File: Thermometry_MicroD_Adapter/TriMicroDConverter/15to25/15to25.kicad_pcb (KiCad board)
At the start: 2 copper layers, 69.1 x 8.7 mm, 3 parts, among them J1 Conn_02x05_Odd_Even, J2 DB15_Male, J4 DB25_Male

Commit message: Updated Gerber
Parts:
- added ?: , , F.Cu at (18.0, 10.0)
- renumbered J4 to J1
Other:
- board text added: "TriMicroDConvert_15Pin_V1 August 2021 Ryan Morgenstern"
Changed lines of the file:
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@@
   (general
     (thickness 1.6)
-    (drawings 4)
+    (drawings 6)
     (tracks 96)
     (zones 0)
-    (modules 3)
+    (modules 4)
     (nets 27)
   )
@@
     (add_net "Net-(J4-Pad13)")
   )
+  (module "" (layer F.Cu)
+    (at 18 10)
+    (fp_text reference "" (at -32 0.55) (layer F.SilkS)
+      (effects (font (size 1.27 1.27) (thickness 0.15)))
+    )
+    (fp_text value "" (at -32 0.55) (layer F.SilkS)
+      (effects (font (size 1.27 1.27) (thickness 0.15)))
+    )
+    (fp_text user J1 (at -50 -7 -180) (layer F.SilkS)
+      (effects (font (size 1.2 1.2) (thickness 0.15)))
+    )
+  )
   (module Connector:Norcomp-380-025-113L001-microd_NoLeads (layer B.Cu)
     (at -32 0.55 180)
     (tags "380-025-213L001 ")
-    (fp_text reference J4 (at 0 -2.71) (layer B.SilkS)
-      (effects (font (size 1.2 1.2) (thickness 0.15)))
+    (fp_text reference J1 (at 0 -2.71) (layer B.SilkS)
+      (effects (font (size 1.2 1.2) (thickness 0.15)) (justify mirror))
     )
     (fp_text value DB25_Male (at 0.365 -6) (layer F.Fab)
       (effects (font (size 1.2 1.2) (thickness 0.15)))
     )
+    (fp_line (start -14.85 3.675) (end -14.85 -3.675) (layer B.CrtYd) (width 0.15))
+    (fp_line (start 14.85 3.675) (end -14.85 3.675) (layer B.CrtYd) (width 0.15))
+    (fp_line (start 14.85 -3.675) (end 14.85 3.675) (layer B.CrtYd) (width 0.15))
+    (fp_line (start -14.85 -3.675) (end 14.85 -3.675) (layer B.CrtYd) (width 0.15))
+    (fp_line (start 9.08 1.51) (end -8.08 1.51) (layer B.SilkS) (width 0.15))
+    (fp_line (start 9.08 -1.51) (end 9.08 1.51) (layer B.SilkS) (width 0.15))
+    (fp_line (start -9.08 -1.51) (end 9.08 -1.51) (layer B.SilkS) (width 0.15))
+    (fp_line (start -9.08 0.51) (end -9.08 -1.51) (layer B.SilkS) (width 0.15))
     (fp_line (start -8.08 1.51) (end -9.08 0.51) (layer B.SilkS) (width 0.15))
-    (fp_line (start -9.08 0.51) (end -9.08 -1.51) (layer B.SilkS) (width 0.15))
-    (fp_line (start -9.08 -1.51) (end 9.08 -1.51) (layer B.SilkS) (width 0.15))
-    (fp_line (start 9.08 -1.51) (end 9.08 1.51) (layer B.SilkS) (width 0.15))
-    (fp_line (start 9.08 1.51) (end -8.08 1.51) (layer B.SilkS) (width 0.15))
-    (fp_line (start -14.85 -3.675) (end 14.85 -3.675) (layer B.CrtYd) (width 0.15))
-    (fp_line (start 14.85 -3.675) (end 14.85 3.675) (layer B.CrtYd) (width 0.15))
-    (fp_line (start 14.85 3.675) (end -14.85 3.675) (layer B.CrtYd) (width 0.15))
-    (fp_line (start -14.85 3.675) (end -14.85 -3.675) (layer B.CrtYd) (width 0.15))
     (fp_text user "Male / Plug" (at 0 2.54) (layer B.Fab)
       (effects (font (size 1.2 1.2) (thickness 0.15)) (justify mirror))
@@
       (rotate (xyz 0 0 180))
     )
+    (model C:/Users/Cir/Downloads/380-025-113L001.STEP
+      (offset (xyz 0 3.6 10.5))
+      (scale (xyz 1 1 1))
+      (rotate (xyz 0 0 0))
+    )
   )
   (module Connector_PinHeader_1.00mm:PinHeader_2x05_P1.00mm_Vertical (layer F.Cu)
@@
     (descr "Through hole straight pin header, 2x05, 1.00mm pitch, double rows")
     (tags "Through hole pin header THT 2x05 1.00mm double row")
-    (fp_text reference J1 (at -1.9 5.8) (layer F.SilkS)
+    (fp_text reference J1 (at 3.07 -0.29) (layer F.SilkS)
       (effects (font (size 1 1) (thickness 0.15)))
     )
@@
       (effects (font (size 1 1) (thickness 0.15)))
     )
+    (fp_line (start -0.075 -0.5) (end 1.65 -0.5) (layer F.Fab) (width 0.1))
+    (fp_line (start 1.65 -0.5) (end 1.65 4.5) (layer F.Fab) (width 0.1))
+    (fp_line (start 1.65 4.5) (end -0.65 4.5) (layer F.Fab) (width 0.1))
+    (fp_line (start -0.65 4.5) (end -0.65 0.075) (layer F.Fab) (width 0.1))
+    (fp_line (start -0.65 0.075) (end -0.075 -0.5) (layer F.Fab) (width 0.1))
+    (fp_line (start -0.71 4.56) (end -0.394493 4.56) (layer F.SilkS) (width 0.12))
+    (fp_line (start 1.394493 4.56) (end 1.71 4.56) (layer F.SilkS) (width 0.12))
+    (fp_line (start 0.394493 4.56) (end 0.605507 4.56) (layer F.SilkS) (width 0.12))
+    (fp_line (start -0.71 0.685) (end -0.71 4.56) (layer F.SilkS) (width 0.12))
+    (fp_line (start 1.71 -0.56) (end 1.71 4.56) (layer F.SilkS) (width 0.12))
+    (fp_line (start -0.71 0.685) (end -0.608276 0.685) (layer F.SilkS) (width 0.12))
+    (fp_line (start 1.394493 -0.56) (end 1.71 -0.56) (layer F.SilkS) (width 0.12))
+    (fp_line (start -0.71 0) (end -0.71 -0.685) (layer F.SilkS) (width 0.12))
+    (fp_line (start -0.71 -0.685) (end 0 -0.685) (layer F.SilkS) (width 0.12))
+    (fp_line (start -1.15 -1) (end -1.15 5) (layer F.CrtYd) (width 0.05))
+    (fp_line (start -1.15 5) (end 2.15 5) (layer F.CrtYd) (width 0.05))
+    (fp_line (start 2.15 5) (end 2.15 -1) (layer F.CrtYd) (width 0.05))
     (fp_line (start 2.15 -1) (end -1.15 -1) (layer F.CrtYd) (width 0.05))
-    (fp_line (start 2.15 5) (end 2.15 -1) (layer F.CrtYd) (width 0.05))
-    (fp_line (start -1.15 5) (end 2.15 5) (layer F.CrtYd) (width 0.05))
-    (fp_line (start -1.15 -1) (end -1.15 5) (layer F.CrtYd) (width 0.05))
-    (fp_line (start -0.71 -0.685) (end 0 -0.685) (layer F.SilkS) (width 0.12))
-    (fp_line (start -0.71 0) (end -0.71 -0.685) (layer F.SilkS) (width 0.12))
-    (fp_line (start 1.394493 -0.56) (end 1.71 -0.56) (layer F.SilkS) (width 0.12))
-    (fp_line (start -0.71 0.685) (end -0.608276 0.685) (layer F.SilkS) (width 0.12))
-    (fp_line (start 1.71 -0.56) (end 1.71 4.56) (layer F.SilkS) (width 0.12))
-    (fp_line (start -0.71 0.685) (end -0.71 4.56) (layer F.SilkS) (width 0.12))
-    (fp_line (start 0.394493 4.56) (end 0.605507 4.56) (layer F.SilkS) (width 0.12))
-    (fp_line (start 1.394493 4.56) (end 1.71 4.56) (layer F.SilkS) (width 0.12))
-    (fp_line (start -0.71 4.56) (end -0.394493 4.56) (layer F.SilkS) (width 0.12))
-    (fp_line (start -0.65 0.075) (end -0.075 -0.5) (layer F.Fab) (width 0.1))
-    (fp_line (start -0.65 4.5) (end -0.65 0.075) (layer F.Fab) (width 0.1))
-    (fp_line (start 1.65 4.5) (end -0.65 4.5) (layer F.Fab) (width 0.1))
-    (fp_line (start 1.65 -0.5) (end 1.65 4.5) (layer F.Fab) (width 0.1))
-    (fp_line (start -0.075 -0.5) (end 1.65 -0.5) (layer F.Fab) (width 0.1))
     (fp_text user %R (at 0.5 2) (layer F.Fab)
       (effects (font (size 1 1) (thickness 0.15)))
@@
       (effects (font (size 1 1) (thickness 0.15)) (justify mirror))
     )
-    (fp_line (start 16.4465 -4.5466) (end 16.4465 3.4544) (layer B.CrtYd) (width 0.05))
-    (fp_line (start -7.5565 -4.5466) (end 16.4465 -4.5466) (layer B.CrtYd) (width 0.05))
-    (fp_line (start -7.5565 3.4544) (end -7.5565 -4.5466) (layer B.CrtYd) (width 0.05))
-    (fp_line (start 16.4465 3.4544) (end -7.5565 3.4544) (layer B.CrtYd) (width 0.05))
+    (fp_line (start -7.4295 -4.4196) (end 16.3195 -4.4196) (layer B.SilkS) (width 0.12))
+    (fp_line (start 16.3195 -4.4196) (end 16.3195 3.3274) (layer B.SilkS) (width 0.12))
+    (fp_line (start 16.3195 3.3274) (end -7.4295 3.3274) (layer B.SilkS) (width 0.12))
+    (fp_line (start -7.4295 3.3274) (end -7.4295 -4.4196) (layer B.SilkS) (width 0.12))
+    (fp_line (start -7.3025 -4.2926) (end 16.1925 -4.2926) (layer B.Fab) (width 0.1))
+    (fp_line (start 16.1925 -4.2926) (end 16.1925 3.2004) (layer B.Fab) (width 0.1))
+    (fp_line (start 16.1925 3.2004) (end -7.3025 3.2004) (layer B.Fab) (width 0.1))
+    (fp_line (start -7.3025 3.2004) (end -7.3025 -4.2926) (layer B.Fab) (width 0.1))
+    (fp_line (start 4.318 3.0734) (end 4.572 3.0734) (layer B.SilkS) (width 0.12))
+    (fp_line (start 4.572 3.0734) (end 4.572 3.3274) (layer B.SilkS) (width 0.12))
+    (fp_line (start 4.572 3.3274) (end 4.318 3.3274) (layer B.SilkS) (width 0.12))
+    (fp_line (start 4.318 3.3274) (end 4.318 3.0734) (layer B.SilkS) (width 0.12))
     (fp_line (start 4.445 3.2004) (end 4.445 3.2004) (layer B.Fab) (width 0.1))
     (fp_line (start 4.445 3.2004) (end 4.445 3.2004) (layer B.Fab) (width 0.1))
     (fp_line (start 4.445 3.2004) (end 4.445 3.2004) (layer B.Fab) (width 0.1))
     (fp_line (start 4.445 3.2004) (end 4.445 3.2004) (layer B.Fab) (width 0.1))
-    (fp_line (start 4.318 3.3274) (end 4.318 3.0734) (layer B.SilkS) (width 0.12))
-    (fp_line (start 4.572 3.3274) (end 4.318 3.3274) (layer B.SilkS) (width 0.12))
-    (fp_line (start 4.572 3.0734) (end 4.572 3.3274) (layer B.SilkS) (width 0.12))
-    (fp_line (start 4.318 3.0734) (end 4.572 3.0734) (layer B.SilkS) (width 0.12))
-    (fp_line (start -7.3025 3.2004) (end -7.3025 -4.2926) (layer B.Fab) (width 0.1))
-    (fp_line (start 16.1925 3.2004) (end -7.3025 3.2004) (layer B.Fab) (width 0.1))
-    (fp_line (start 16.1925 -4.2926) (end 16.1925 3.2004) (layer B.Fab) (width 0.1))
-    (fp_line (start -7.3025 -4.2926) (end 16.1925 -4.2926) (layer B.Fab) (width 0.1))
-    (fp_line (start -7.4295 3.3274) (end -7.4295 -4.4196) (layer B.SilkS) (width 0.12))
-    (fp_line (start 16.3195 3.3274) (end -7.4295 3.3274) (layer B.SilkS) (width 0.12))
-    (fp_line (start 16.3195 -4.4196) (end 16.3195 3.3274) (layer B.SilkS) (width 0.12))
-    (fp_line (start -7.4295 -4.4196) (end 16.3195 -4.4196) (layer B.SilkS) (width 0.12))
+    (fp_line (start 16.4465 3.4544) (end -7.5565 3.4544) (layer B.CrtYd) (width 0.05))
+    (fp_line (start -7.5565 3.4544) (end -7.5565 -4.5466) (layer B.CrtYd) (width 0.05))
+    (fp_line (start -7.5565 -4.5466) (end 16.4465 -4.5466) (layer B.CrtYd) (width 0.05))
+    (fp_line (start 16.4465 -4.5466) (end 16.4465 3.4544) (layer B.CrtYd) (width 0.05))
     (fp_text user * (at -2.54 0) (layer B.Fab)
       (effects (font (size 1 1) (thickness 0.15)) (justify mirror))
@@
     )
   )
+  (gr_text "TriMicroDConvert_15Pin_V1\nAugust 2021\nRyan Morgenstern" (at -51.66 3.41) (layer B.SilkS)
+    (effects (font (size 0.4 0.4) (thickness 0.1)) (justify mirror))
+  )
+  (gr_text "TriMicroDConvert_15Pin_V1\nAugust 2021\nRyan Morgenstern" (at -51.4 3.36) (layer F.SilkS)
+    (effects (font (size 0.4 0.4) (thickness 0.1)))
+  )
   (gr_line (start -56.1 -3.8) (end 13 -3.8) (layer Edge.Cuts) (width 0.15))

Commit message: update
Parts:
- renumbered J1 to J4
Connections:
- J4 pad 3: Net-(J2-Pad3) -> Net-(J2-Pad4)
- J4 pad 4: Net-(J2-Pad4) -> Net-(J2-Pad5)
- J4 pad 5: Net-(J2-Pad5) -> Net-(J2-Pad6)
- J4 pad 6: Net-(J2-Pad6) -> Net-(J2-Pad7)
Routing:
- net Net-(J2-Pad7): track 0.00 -> 37.3 mm
- net Net-(J2-Pad3): track 27.5 -> 0.00 mm
- net Net-(J2-Pad4): track 30.6 -> 29.2 mm
- net Net-(J2-Pad1): track 21.3 -> 22.4 mm
- net Net-(J2-Pad6): track 35.5 -> 34.6 mm
- net Net-(J2-Pad5): track 32.8 -> 31.9 mm
- net Net-(J1-Pad2): track 23.3 -> 23.9 mm
- net Net-(J1-Pad1): track 23.9 -> 24.5 mm
- net Net-(J1-Pad10): track 13.6 -> 13.0 mm
- net Net-(J2-Pad11): track 28.7 -> 29.3 mm
- net Net-(J2-Pad9): track 23.4 -> 23.9 mm
- net Net-(J2-Pad2): track 24.8 -> 25.3 mm
- net Net-(J2-Pad8): track 39.5 -> 40.0 mm
- net Net-(J2-Pad10): track 26.0 -> 26.5 mm
- net Net-(J2-Pad12): track 31.4 -> 31.9 mm
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
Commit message: update
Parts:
- removed ?: , 
- added J3: Conn_01x04, Connector_JST:JST_PH_B4B-PH-K_1x04_P2.00mm_Vertical, F.Cu at (-62.5, 0.00)
- added J5: Conn_01x02, Connector_PinHeader_1.00mm:PinHeader_1x02_P1.00mm_Vertical, F.Cu at (-51.1, 0.01)
- J1: value Conn_02x05_Odd_Even -> Conn_01x04; footprint Connector_PinHeader_1.00mm:PinHeader_2x05_P1.00mm_Vertical -> Connector_JST:JST_PH_B4B-PH-K_1x04_P2.00mm_Vertical
- moved J1 21.0 mm to (-75.5, 0.00), turned to 0 degrees
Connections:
- J4 pad 10: Net-(J1-Pad5) -> Net-(J3-Pad1)
- J4 pad 11: Net-(J1-Pad7) -> Net-(J3-Pad3)
- J4 pad 12: Net-(J1-Pad9) -> Net-(J4-Pad12)
- J4 pad 23: Net-(J1-Pad6) -> Net-(J3-Pad2)
- J4 pad 24: Net-(J1-Pad8) -> Net-(J3-Pad4)
- J4 pad 25: Net-(J1-Pad10) -> Net-(J4-Pad25)
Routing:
- net Net-(J3-Pad1): track 0.00 -> 28.4 mm
- net Net-(J3-Pad2): track 0.00 -> 26.2 mm
- net Net-(J3-Pad3): track 0.00 -> 23.0 mm
- net Net-(J3-Pad4): track 0.00 -> 20.8 mm
- net Net-(J1-Pad1): track 24.5 -> 44.2 mm
- net Net-(J1-Pad5): track 19.1 -> 0.00 mm
- net Net-(J1-Pad6): track 18.4 -> 0.00 mm
- net Net-(J1-Pad2): track 23.9 -> 42.1 mm
- net Net-(J1-Pad3): track 21.8 -> 38.8 mm
- net Net-(J1-Pad7): track 16.4 -> 0.00 mm
- net Net-(J1-Pad8): track 15.7 -> 0.00 mm
- net Net-(J1-Pad4): track 21.2 -> 36.6 mm
- net Net-(J1-Pad9): track 14.3 -> 0.00 mm
- net Net-(J4-Pad12): track 0.00 -> 14.2 mm
- net Net-(J4-Pad25): track 0.00 -> 13.7 mm
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- added copper zone on F.Cu, net GND
- added copper zone on B.Cu, net Net-(J2-Pad12)
- removed copper zone on B.Cu, net (none)
- removed copper zone on F.Cu, net (none)
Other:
- board size 69.1 x 8.7 mm -> 91.9 x 8.7 mm
- board text added: "TriMicroDConvert_15Pin_V2 July 2022 Ryan Morgenstern"
- board text removed: "TriMicroDConvert_15Pin_V1 August 2021 Ryan Morgenstern"

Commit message: Update
Added current versions of adapter boards.
Added heater line splitter
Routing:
- added copper zone on In1.Cu, net GND
- added copper zone on In2.Cu, net GND
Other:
- copper layers 2 -> 4
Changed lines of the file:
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@@
   (layers
     (0 F.Cu signal)
+    (1 In1.Cu signal)
+    (2 In2.Cu signal)
     (31 B.Cu signal)
     (32 B.Adhes user)
@@
     (47 F.CrtYd user)
     (48 B.Fab user)
-    (49 F.Fab user hide)
+    (49 F.Fab user)
   )
   (setup
@@
       )
     )
+  )
+  (zone (net 21) (net_name GND) (layer In1.Cu) (hatch edge 0.508)
+    (connect_pads (clearance 0.4))
+    (min_thickness 0.254)
+    (fill yes (arc_segments 32) (thermal_gap 0.508) (thermal_bridge_width 0.508))
+    (polygon
+      (pts
+        (xy 16.8 9) (xy -80.5 9) (xy -80.5 -6.7) (xy 16.7 -6.7)
+      )
+    )
+  )
+  (zone (net 21) (net_name GND) (layer In2.Cu) (hatch edge 0.508)
+    (connect_pads (clearance 0.4))
+    (min_thickness 0.254)
+    (fill yes (arc_segments 32) (thermal_gap 0.508) (thermal_bridge_width 0.508))
+    (polygon
+      (pts
+        (xy 15.9 8) (xy -80.5 8) (xy -80.5 -6.9) (xy 15.9 -6.9)
+      )
+    )

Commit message: update
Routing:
- net Net-(J2-Pad6): track 34.8 -> 34.1 mm
- net Net-(J2-Pad5): track 32.0 -> 31.4 mm
- net Net-(J2-Pad8): track 40.2 -> 39.6 mm
- net Net-(J2-Pad7): track 37.4 -> 36.9 mm
- removed copper zone on In1.Cu, net GND
- removed copper zone on In2.Cu, net GND
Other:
- copper layers 4 -> 2
- net class Default: trace_width 0.09 -> 0.135

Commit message: update
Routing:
- added copper zone on B.Cu, net GND
- removed copper zone on B.Cu, net Net-(J2-Pad12)
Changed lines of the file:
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@@
     (mod_text_size 1 1)
     (mod_text_width 0.15)
-    (pad_size 1.1 1.1)
-    (pad_drill 0.61)
+    (pad_size 3.6 3.6)
+    (pad_drill 2.2606)
     (pad_to_mask_clearance 0)
     (aux_axis_origin 0 0)
@@
   (segment (start -49.34 -1.8) (end -51.15 0.01) (width 0.135) (layer F.Cu) (net 27))
   (segment (start -40.15 -1.8) (end -49.34 -1.8) (width 0.135) (layer F.Cu) (net 27))
-  (zone (net 8) (net_name "Net-(J2-Pad12)") (layer B.Cu) (hatch edge 0.508)
+  (zone (net 21) (net_name GND) (layer B.Cu) (hatch edge 0.508)
     (connect_pads (clearance 0.2))
     (min_thickness 0.254)

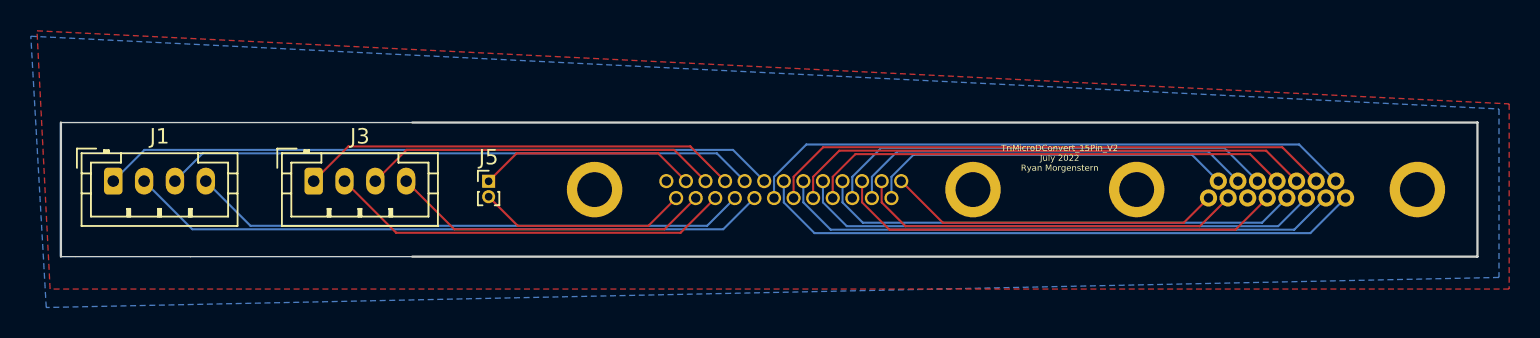
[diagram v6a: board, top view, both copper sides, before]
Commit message: Fixed Error in board. Added diagrams
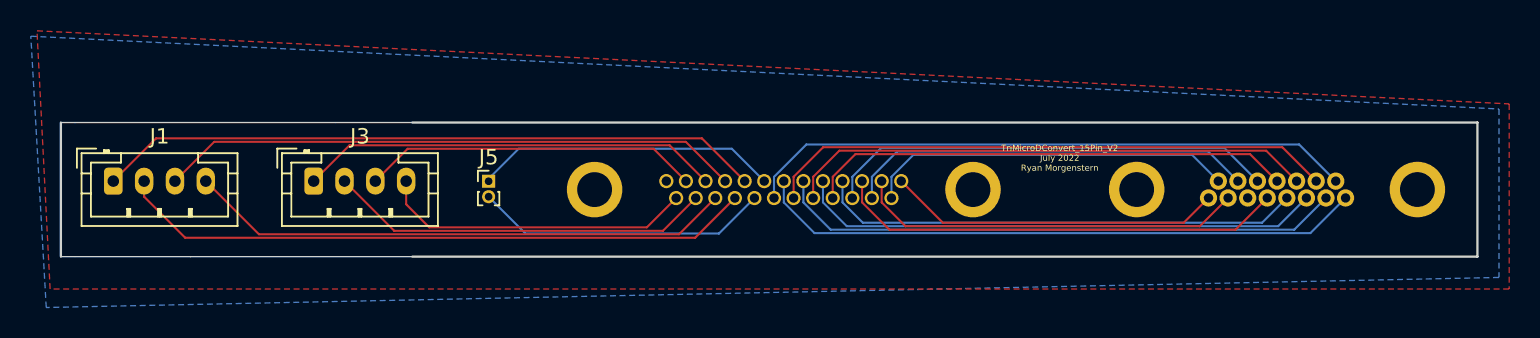
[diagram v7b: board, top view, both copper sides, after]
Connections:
- J4 pad 10: Net-(J3-Pad1) -> Net-(J1-Pad3)
- J4 pad 11: Net-(J3-Pad3) -> Net-(J3-Pad1)
- J4 pad 12: Net-(J4-Pad12) -> Net-(J3-Pad3)
- J4 pad 21: Net-(J1-Pad2) -> Net-(J4-Pad21)
- J4 pad 22: Net-(J1-Pad4) -> Net-(J1-Pad2)
- J4 pad 23: Net-(J3-Pad2) -> Net-(J1-Pad4)
- J4 pad 24: Net-(J3-Pad4) -> Net-(J3-Pad2)
- J4 pad 25: Net-(J4-Pad25) -> Net-(J3-Pad4)
- J4 pad 8: Net-(J1-Pad1) -> Net-(J4-Pad8)
- J4 pad 9: Net-(J1-Pad3) -> Net-(J1-Pad1)
- J5 pad 1: Net-(J4-Pad12) -> Net-(J4-Pad8)
- J5 pad 2: Net-(J4-Pad25) -> Net-(J4-Pad21)
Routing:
- net Net-(J4-Pad8): track 0.00 -> 19.7 mm
- net Net-(J4-Pad21): track 0.00 -> 19.2 mm
- net Net-(J4-Pad12): track 14.3 -> 0.00 mm
- net Net-(J4-Pad25): track 13.7 -> 0.00 mm
- net Net-(J3-Pad2): track 26.4 -> 25.0 mm
- net Net-(J3-Pad3): track 23.1 -> 21.9 mm
- net Net-(J3-Pad1): track 28.6 -> 27.3 mm
- net Net-(J1-Pad4): track 36.3 -> 35.5 mm
- net Net-(J1-Pad3): track 38.5 -> 37.8 mm
- net Net-(J1-Pad1): track 43.9 -> 43.3 mm
